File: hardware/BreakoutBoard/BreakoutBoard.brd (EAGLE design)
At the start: 90 x 56 mm, 38 parts, among them J1 CON-71741-2184-TOP, J10 CON-2X3-RASTER, J11 CON-2X3-RASTER, J12 CON-2X3-RASTER, J13 CON-2X4-RASTER, J2 CON-71741-2184-BOT, J3 CON-2X4-RASTER, J4 CON-2X10-RASTER, J5 CON-2X3-RASTER, J6 CON-2X3-RASTER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

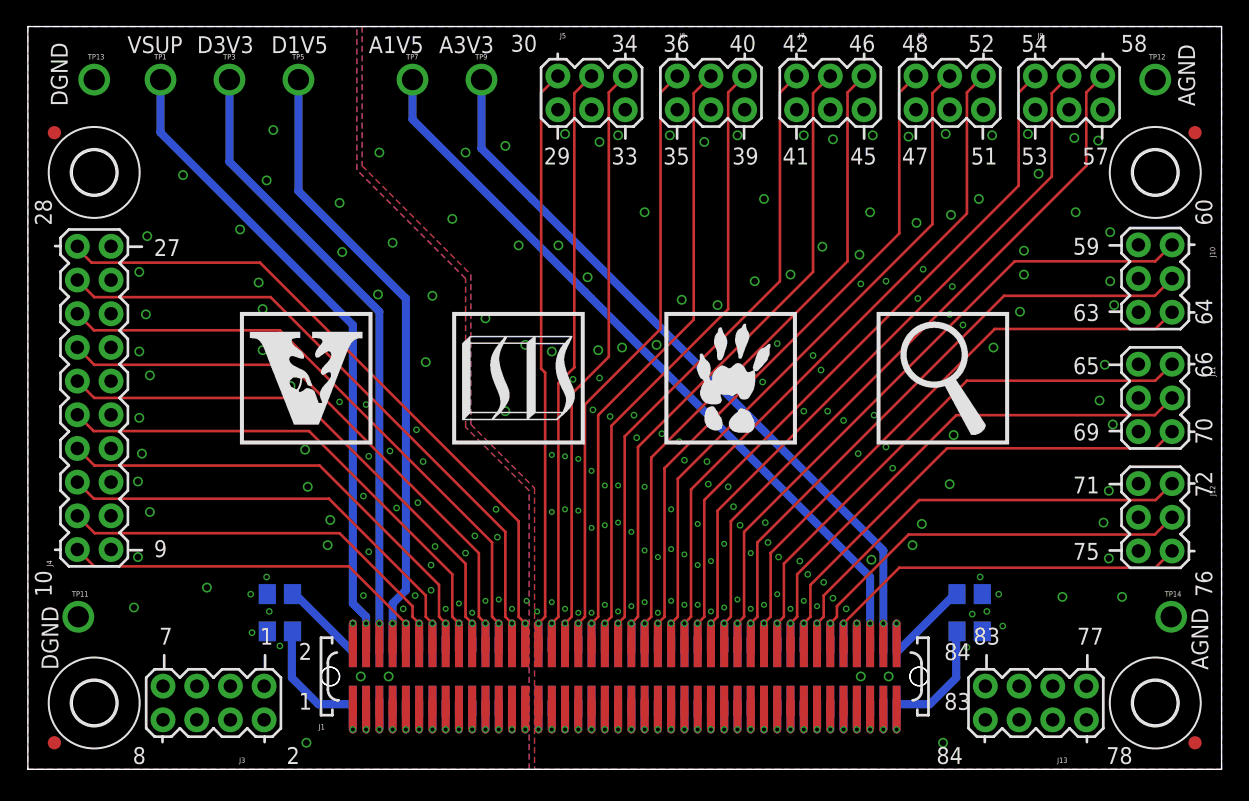
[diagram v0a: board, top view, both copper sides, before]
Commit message: - Fiducials in both sides
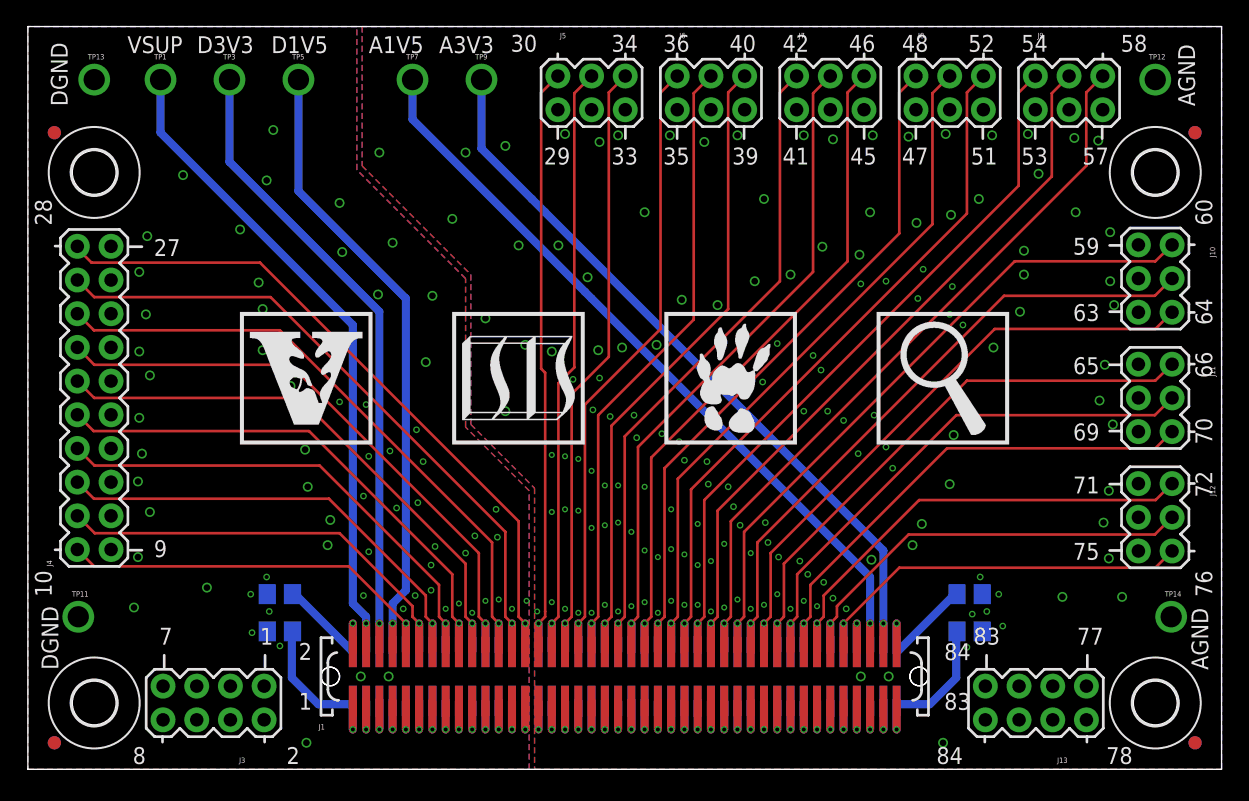
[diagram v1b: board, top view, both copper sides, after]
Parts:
- added M10, M11, M12, M9: FIDUCIAL1X2, powerboard:FIDUCIAL-1X2
